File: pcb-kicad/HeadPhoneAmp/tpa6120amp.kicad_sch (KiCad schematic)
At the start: 11 parts, among them U5 TPA6120A2RGY

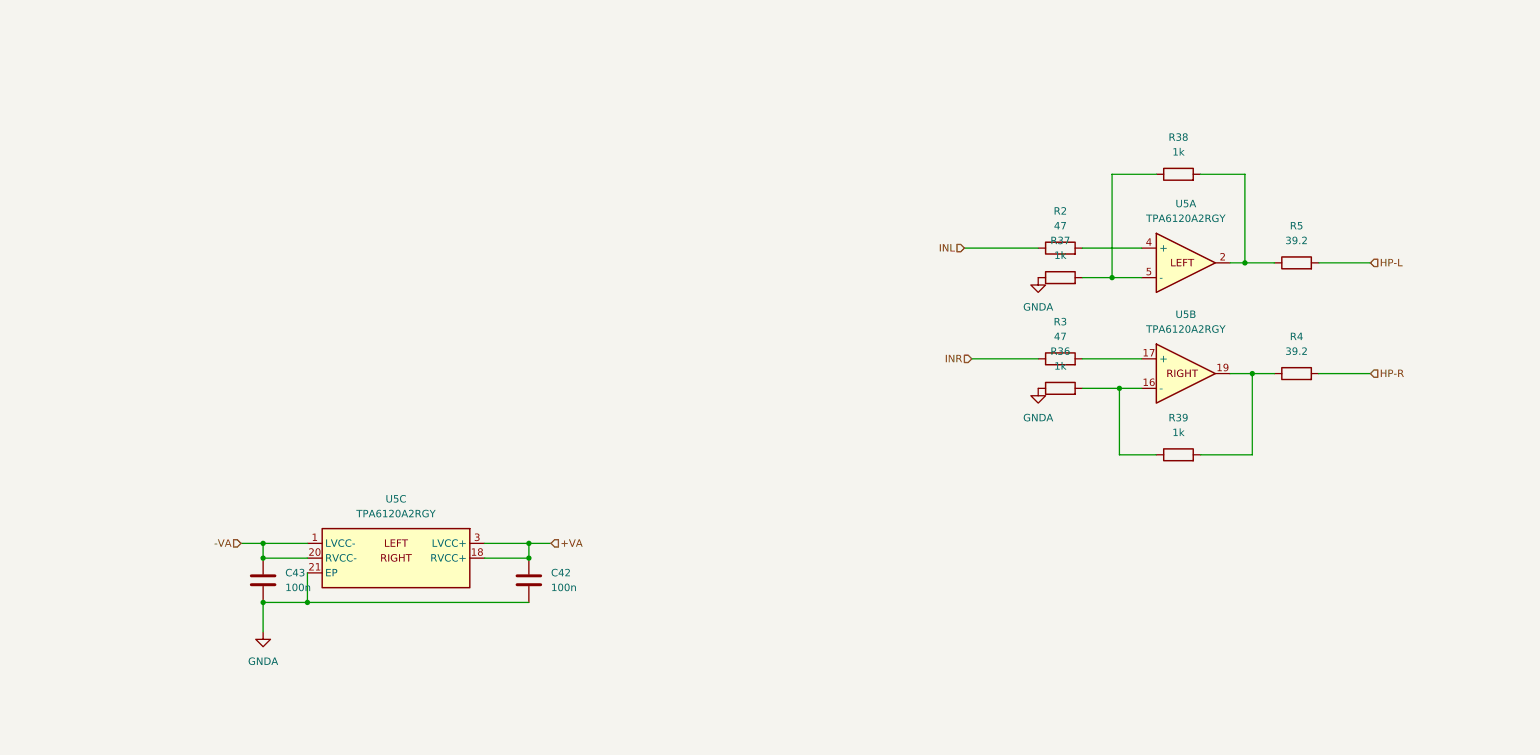
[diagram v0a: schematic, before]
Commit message: Added TPA6120 breakout.
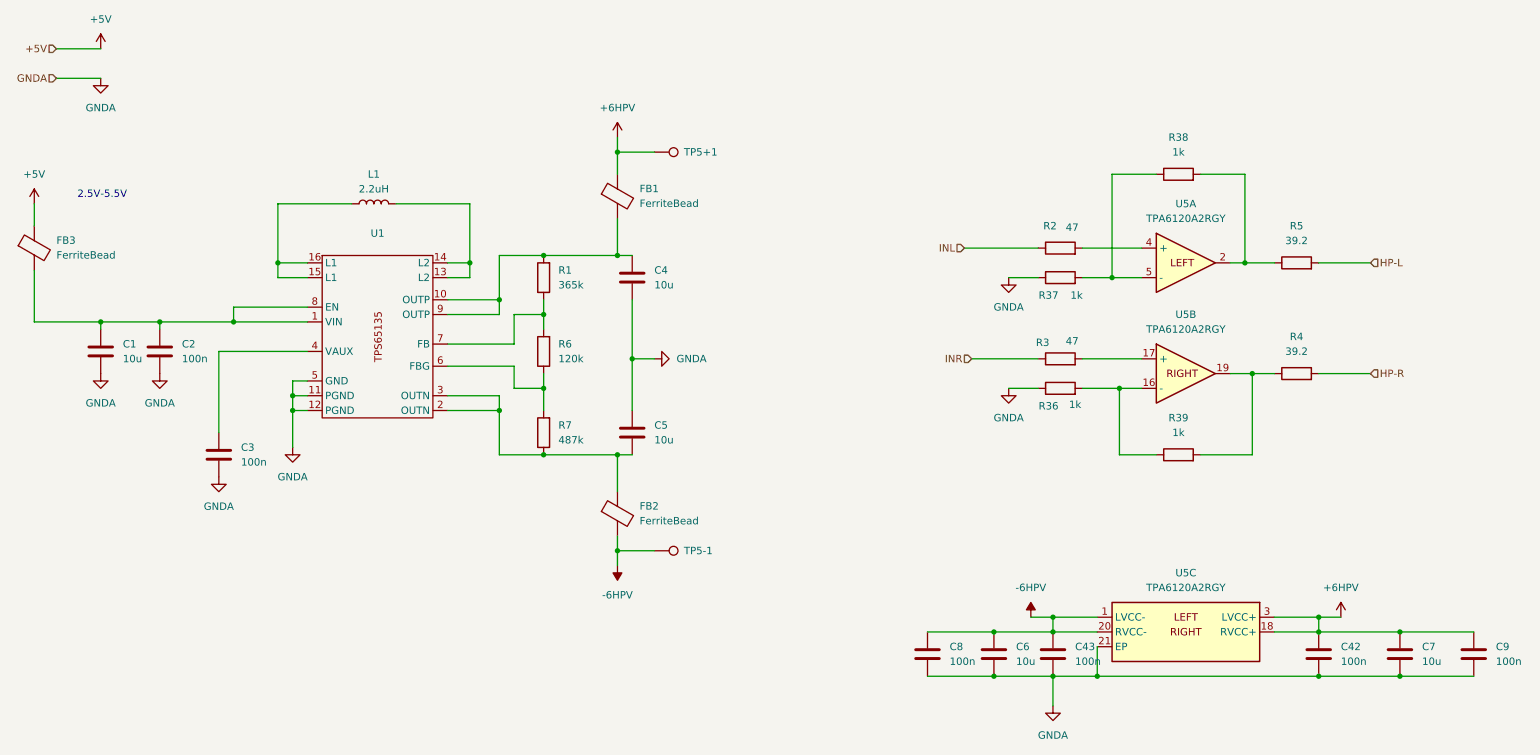
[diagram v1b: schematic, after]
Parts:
- added C1, C4, C5, C6, C7: 10u, Capacitor_SMD:C_0603_1608Metric_Pad1.08x0.95mm_HandSolder, symbol Device:C
- added C2, C3, C8, C9: 100n, Capacitor_SMD:C_0603_1608Metric_Pad1.08x0.95mm_HandSolder, symbol Device:C
- added FB1, FB2, FB3: FerriteBead, Inductor_SMD:L_0603_1608Metric_Pad1.05x0.95mm_HandSolder, symbol Device:FerriteBead
- added L1: 2.2uH, Inductor_SMD:L_1812_4532Metric_Pad1.30x3.40mm_HandSolder, symbol Device:L
- added R1: 365k, Resistor_SMD:R_0603_1608Metric_Pad0.98x0.95mm_HandSolder, symbol Device:R
- added R6: 120k, Resistor_SMD:R_0603_1608Metric_Pad0.98x0.95mm_HandSolder, symbol Device:R
- added R7: 487k, Resistor_SMD:R_0603_1608Metric_Pad0.98x0.95mm_HandSolder, symbol Device:R
- added TP5+1, TP5-1: TestPoint, TestPoint:TestPoint_Pad_2.0x2.0mm, symbol Connector:TestPoint
- added U1: ~, HPAmp:WQFN-16-1EP_3x3mm_P0.5mm_LongPad_ThermalVia, symbol HPAmp:TPS65135
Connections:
- net -VA is gone; now on net -6HPV: C43.1, U5.1 (LVCC-), U5.20 (RVCC-)
- net GNDA: now also C1.2, C2.2, C3.2, C4.2, C5.1, C6.2, C7.2, C8.2, C9.2, U1.11 (PGND), U1.12 (PGND), U1.5 (GND)
- net -6HPV: now reaches U5.20 (RVCC-)
- net -6HPV: now also C6.1, C8.1, FB2.2, TP5-1.1
- net +VA renamed +6HPV
- net +6HPV: now also C7.1, C9.1, FB1.1, TP5+1.1
- new net: L1.1, U1.15 (L1), U1.16 (L1)
- new net: L1.2, U1.13 (L2), U1.14 (L2)
- new net: C4.1, FB1.2, R1.2, U1.10 (OUTP), U1.9 (OUTP)
- new net: C5.2, FB2.1, R7.1, U1.2 (OUTN), U1.3 (OUTN)
- new net: R6.1, R7.2, U1.6 (FBG)
- new net: R1.1, R6.2, U1.7 (FB)
- new net: C1.1, C2.1, FB3.2, U1.1 (VIN), U1.8 (EN)
- new net: C3.1, U1.4 (VAUX)
- new net +5V: FB3.1
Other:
- note added: "2.5V-5.5V"
- moved on the sheet: C42, C43, U5C

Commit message: Added some order infos.
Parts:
- C1, C2, C3, C4, C42, C43, C5, C6, C7, C8, C9, FB1, FB2, FB3, R36, R37, R38, R39, U5: MFNAME (none) -> -
- L1: MFNAME (none) -> CC453232-2R2KL
- R1: MFNAME (none) -> RK73H1JTTD3653F
- R2, R3: MFNAME (none) -> RK73H1JTTD47R0F
- R4, R5: MFNAME (none) -> RK73H3ATTE39R2F
- R6: MFNAME (none) -> RK73H1JTTD1203F
- R7: MFNAME (none) -> RK73H1JTTD4873F
- TP5+1, TP5-1: value TestPoint -> ~; MFNAME (none) -> -
- U1: value ~ -> TPS65135; MFNAME (none) -> -

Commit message: HPBooster v0.2, changed TPA footprint.
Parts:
- U5: footprint Package_SO:HSOP-20-1EP_11.0x15.9mm_P1.27mm_SlugDown_ThermalVias -> Package_SO:SOP-20_7.5x12.8mm_P1.27mm
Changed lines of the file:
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@@
 			)
 		)
-		(property "Footprint" "Package_SO:HSOP-20-1EP_11.0x15.9mm_P1.27mm_SlugDown_ThermalVias"
+		(property "Footprint" "Package_SO:SOP-20_7.5x12.8mm_P1.27mm"
 			(at 218.44 119.38 0)
 			(effects
@@
 			)
 		)
-		(property "Footprint" "Package_SO:HSOP-20-1EP_11.0x15.9mm_P1.27mm_SlugDown_ThermalVias"
+		(property "Footprint" "Package_SO:SOP-20_7.5x12.8mm_P1.27mm"
 			(at 187.96 133.35 0)
 			(effects
@@
 			)
 		)
-		(property "Footprint" "Package_SO:HSOP-20-1EP_11.0x15.9mm_P1.27mm_SlugDown_ThermalVias"
+		(property "Footprint" "Package_SO:SOP-20_7.5x12.8mm_P1.27mm"
 			(at 218.44 100.33 0)
 			(effects
